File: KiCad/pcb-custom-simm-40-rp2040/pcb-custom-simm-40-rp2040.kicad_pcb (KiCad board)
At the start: 2 copper layers, 42 parts, among them IC1 W25Q16JVUXIQ_TR, IC2 RT6150B-33GQW, IC3 RP2040, Q1 DMG1012T, SW1 SW_Push_Dual, Y1 12MHz

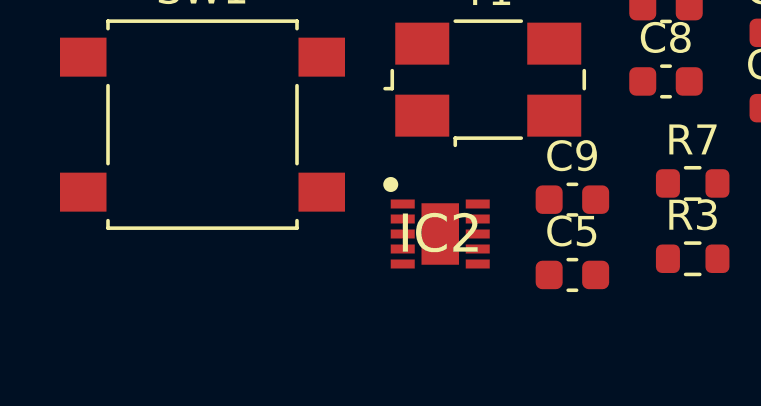
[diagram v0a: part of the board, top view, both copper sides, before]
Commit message: Add custom footprint to project. Update schematics, layout and documents
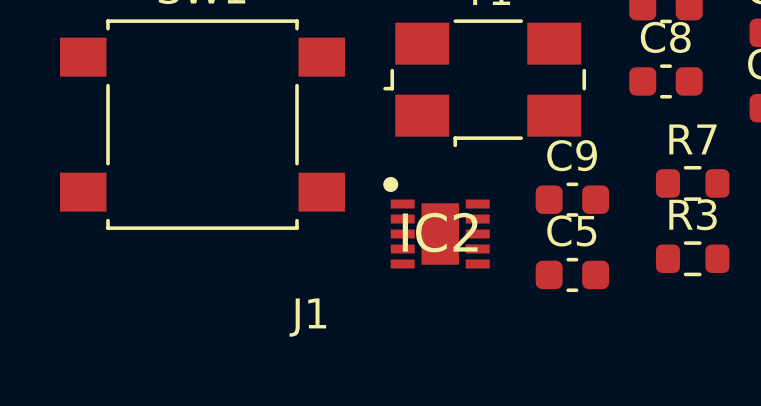
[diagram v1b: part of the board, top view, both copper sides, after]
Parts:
- added J1: SIMM-40 Connector, Custom:MySIMM_40, F.Cu at (147.0, 108.5)
